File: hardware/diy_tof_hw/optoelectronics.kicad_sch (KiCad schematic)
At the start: 39 parts, among them IC21 74LVC1G08QW5-7, IC22 LMG1025QDEETQ1, SW2 SW_Nidec_CAS-120A1, U2 OPA858xDSG, U3 TLV3501AIDBV

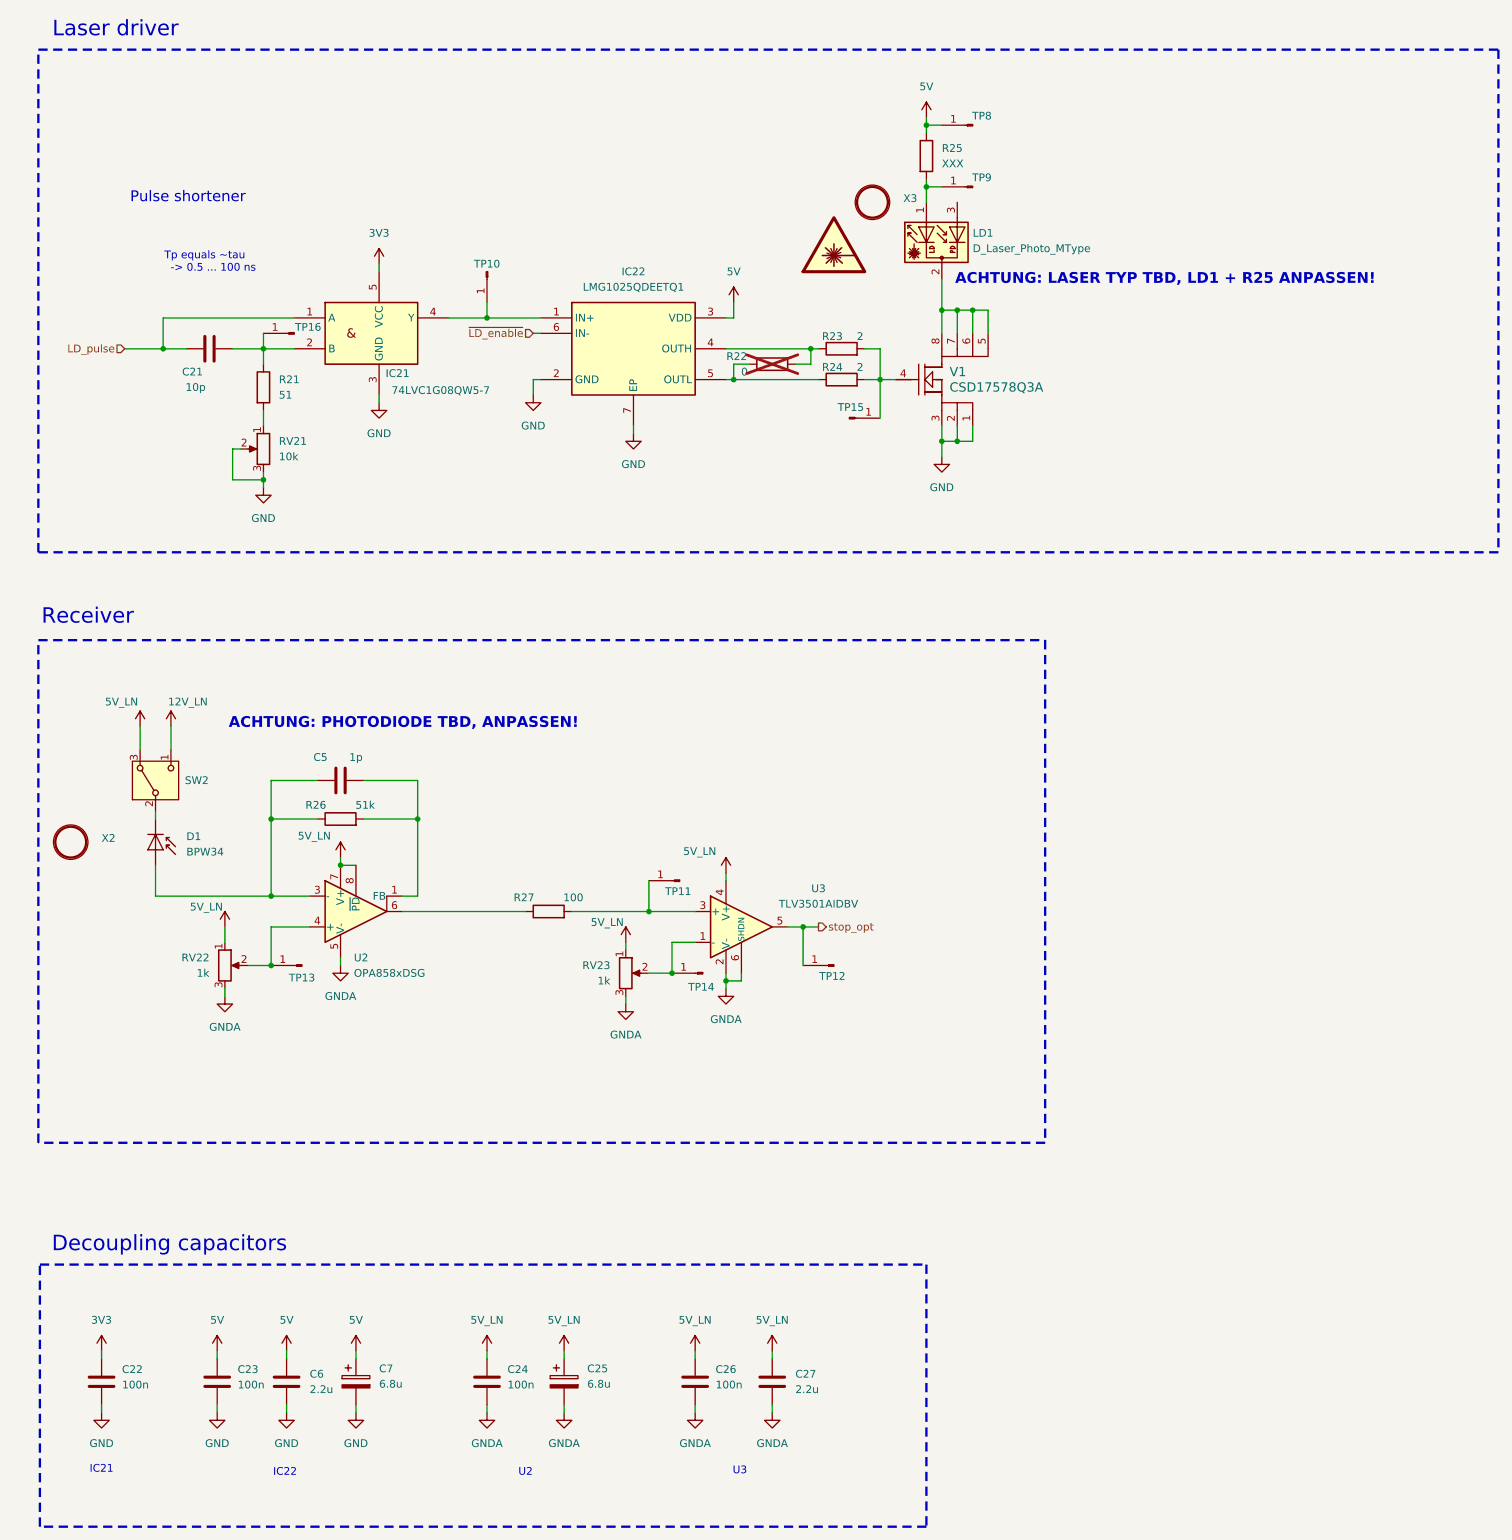
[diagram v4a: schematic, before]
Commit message: [hardware] added VCSEL, photodiode and some pcb graphics to the project
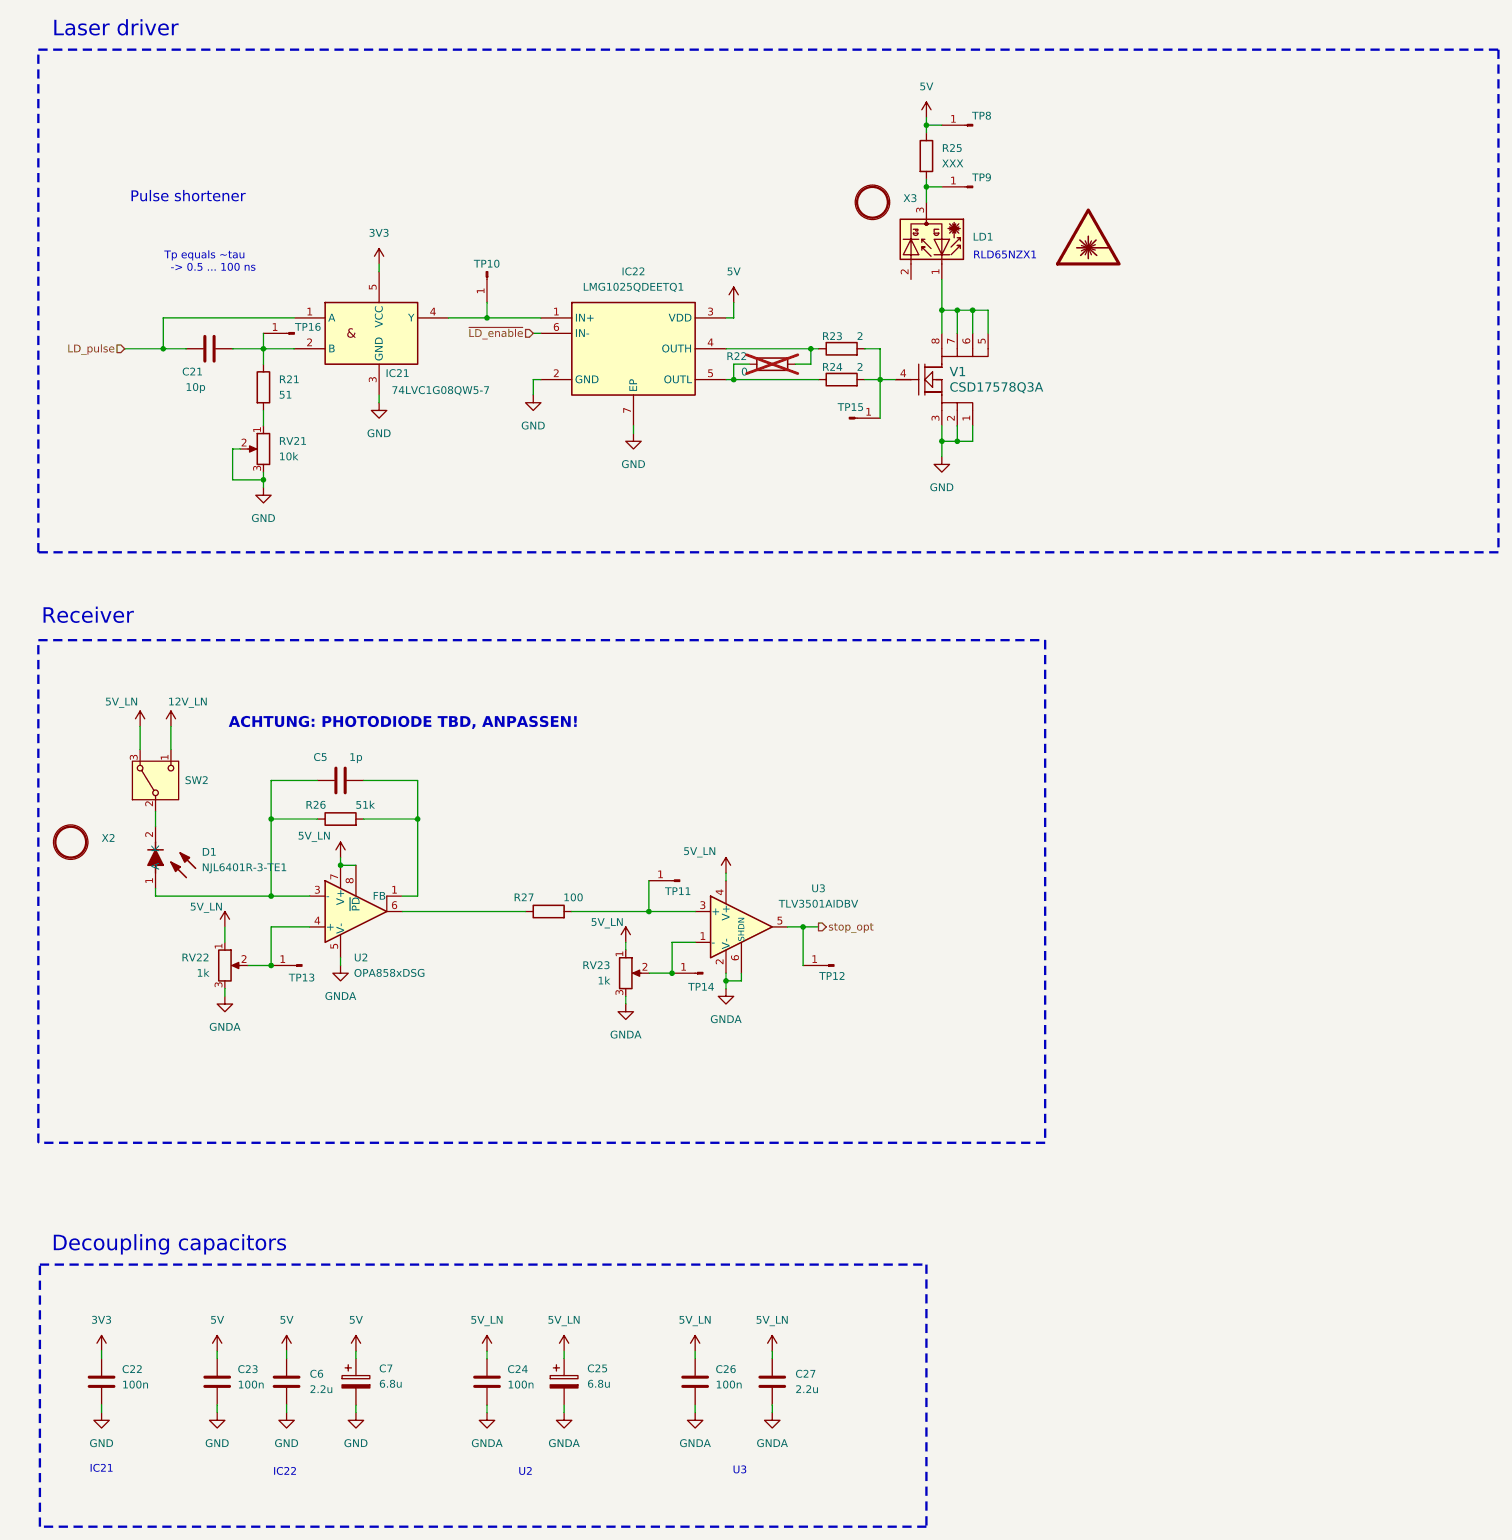
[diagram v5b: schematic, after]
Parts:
- removed D1: BPW34, OptoDevice:Osram_DIL2_4.3x4.65mm_P5.08mm, symbol Sensor_Optical:BPW34
- removed LD1: D_Laser_Photo_MType, OptoDevice:LaserDiode_TO5-D9-3, symbol Device:D_Laser_Photo_MType
- added D1: NJL6401R-3-TE1, NJL6401R3TE1, symbol NJL6401R-3-TE1:NJL6401R-3-TE1
- added LD1: ~, RLD65NZX1-00A:RLD85PZJ400A, symbol RLD65NZX1-00A:RLD65NZX1
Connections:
- net at C5.1, R26.1, U2.3 (-): now also D1.1 (A)
- net at SW2.2 (B): now also D1.2 (K)
- net at R25.2, TP9.1 (Pin_1): now also LD1.3
- net at V1.5, V1.6, V1.7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: now also LD1.1
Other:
- note added: "RLD65NZX1"
- note removed: "ACHTUNG: LASER TYP TBD, LD1 + R25 ANPASSEN!"
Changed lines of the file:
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@@
 	(wire
 		(pts
-			(xy 66.04 144.78) (xy 66.04 146.05)
+			(xy 66.04 144.78) (xy 66.04 147.32)
 		)
 		(stroke
@@
 	(wire
 		(pts
-			(xy 66.04 153.67) (xy 66.04 158.75)
-		)
-		(stroke
-			(width 0)
-			(type default)
-		)
-	)
-	(wire
-		(pts
 			(xy 173.99 68.58) (xy 175.26 68.58)
 		)
@@
 	(wire
 		(pts
+			(xy 66.04 157.48) (xy 66.04 158.75)
+		)
+		(stroke
+			(width 0)
+			(type default)
+		)
+	)
+	(wire
+		(pts
 			(xy 198.12 83.82) (xy 195.58 83.82)
 		)
@@
 		)
 	)
-	(text "ACHTUNG: LASER TYP TBD, LD1 + R25 ANPASSEN!"
-		(exclude_from_sim no)
-		(at 232.41 57.15 0)
-		(effects
-			(font
-				(size 1.778 1.778)
-				(thickness 0.3556)
-				(bold yes)
-				(color 255 36 34 1)
-			)
-		)
-	)
 	(text "U2"
 		(exclude_from_sim no)
@@
 		)
 	)
+	(text "RLD65NZX1"
+		(exclude_from_sim no)
+		(at 205.994 53.34 0)
+		(effects
+			(font
+				(size 1.27 1.27)
+			)
+		)
+	)
 	(text "IC22"
 		(exclude_from_sim no)
@@
 	)
 	(symbol
+		(lib_id "RLD65NZX1-00A:RLD65NZX1")
+		(at 193.04 50.8 270)
+		(unit 1)
+		(exclude_from_sim no)
+		(in_bom yes)
+		(on_board yes)
+		(dnp no)
+		(fields_autoplaced yes)
+		(property "Reference" "LD1"
+			(at 200.66 50.1649 90)
+			(effects
+				(font
+					(size 1.27 1.27)
+				)
+				(justify left)
+			)
+		)
+		(property "Value" "~"
+			(at 200.66 52.07 90)
+			(effects
+				(font
+					(size 1.27 1.27)
+				)
+				(justify left)
+			)
+		)
+		(property "Footprint" "RLD65NZX1-00A:RLD85PZJ400A"
+			(at 193.04 50.8 0)
+			(effects
+				(font
+					(size 1.27 1.27)
+				)
+				(hide yes)
+			)
+		)
+		(property "Datasheet" ""
+			(at 193.04 50.8 0)
+			(effects
+				(font
+					(size 1.27 1.27)
+				)
+				(hide yes)
+			)
+		)
+		(property "Description" ""
+			(at 193.04 50.8 0)
+			(effects
+				(font
+					(size 1.27 1.27)
+				)
+				(hide yes)
+			)
+		)
+		(pin "1"
+		)
+		(pin "2"
+		)
+		(pin "3"
+		)
+		(instances
+			(project ""
+				(path "/0f7bf370-0a80-4101-a61d-d850fd66ab1d/1536e9f2-3315-42ae-af66-5ae730c43aea"
+					(reference "LD1")
+					(unit 1)
+				)
+			)
+		)
+	)
+	(symbol
 		(lib_id "Device:C")
 		(at 154.94 238.76 0)
@@
 	)
 	(symbol
-		(lib_id "Sensor_Optical:BPW34")
-		(at 66.04 151.13 270)
-		(unit 1)
-		(exclude_from_sim no)
-		(in_bom yes)
-		(on_board yes)
-		(dnp no)
-		(fields_autoplaced yes)
-		(property "Reference" "D1"
-			(at 71.12 148.9328 90)
-			(effects
-				(font
-					(size 1.27 1.27)
-				)
-				(justify left)
-			)
-		)
-		(property "Value" "BPW34"
-			(at 71.12 151.4728 90)
-			(effects
-				(font
-					(size 1.27 1.27)
-				)
-				(justify left)
-			)
-		)
-		(property "Footprint" "OptoDevice:Osram_DIL2_4.3x4.65mm_P5.08mm"
-			(at 70.485 151.13 0)
-			(effects
-				(font
-					(size 1.27 1.27)
-				)
-				(hide yes)
-			)
-		)
-		(property "Datasheet" "http://www.vishay.com/docs/81521/bpw34.pdf"
-			(at 66.04 149.86 0)
-			(effects
-				(font
-					(size 1.27 1.27)
-				)
-				(hide yes)
-			)
-		)
-		(property "Description" "Silicon PIN Photodiode"
-			(at 66.04 151.13 0)
-			(effects
-				(font
-					(size 1.27 1.27)
-				)
-				(hide yes)
-			)
-		)
-		(pin "1"
-		)
-		(pin "2"
-		)
-		(instances
-			(project "diy_tof_hw"
-				(path "/0f7bf370-0a80-4101-a61d-d850fd66ab1d/1536e9f2-3315-42ae-af66-5ae730c43aea"
-					(reference "D1")
-					(unit 1)
-				)
-			)
-		)
-	)
-	(symbol
 		(lib_id "Connector:Conn_01x01_Pin")
 		(at 120.65 55.88 270)
@@
 	)
 	(symbol
-		(lib_id "Device:D_Laser_Photo_MType")
-		(at 195.58 52.07 90)
-		(unit 1)
-		(exclude_from_sim no)
-		(in_bom yes)
-		(on_board yes)
-		(dnp no)
-		(property "Reference" "LD1"
-			(at 200.66 49.5299 90)
-			(effects
-				(font
-					(size 1.27 1.27)
-				)
-				(justify right)
-			)
-		)
-		(property "Value" "D_Laser_Photo_MType"
-			(at 200.66 52.0699 90)
-			(effects
-				(font
-					(size 1.27 1.27)
-				)
-				(justify right)
-			)
-		)
-		(property "Footprint" "OptoDevice:LaserDiode_TO5-D9-3"
-			(at 193.675 51.054 0)
-			(effects
-				(font
-					(size 1.27 1.27)
-				)
-				(hide yes)
-			)
-		)
-		(property "Datasheet" "http://www.egismos.disonhu.com/laser/diode-package.htm"
-			(at 198.12 49.784 0)
-			(effects
-				(font
-					(size 1.27 1.27)
-				)
-				(hide yes)
-			)
-		)
-		(property "Description" "Laser diode with photodiode, common cathode on pin 2"
-			(at 195.58 52.07 0)
-			(effects
-				(font
-					(size 1.27 1.27)
-				)
-				(hide yes)
-			)
-		)
-		(pin "1"
-		)
-		(pin "2"
-		)
-		(pin "3"
-		)
-		(instances
-			(project ""
-				(path "/0f7bf370-0a80-4101-a61d-d850fd66ab1d/1536e9f2-3315-42ae-af66-5ae730c43aea"
-					(reference "LD1")
-					(unit 1)
-				)
-			)
-		)
-	)
-	(symbol
 		(lib_id "power:GNDA")
 		(at 167.64 243.84 0)
@@
 	)
 	(symbol
+		(lib_id "NJL6401R-3-TE1:NJL6401R-3-TE1")
+		(at 66.04 157.48 180)
+		(unit 1)
+		(exclude_from_sim no)
+		(in_bom yes)
+		(on_board yes)
+		(dnp no)
+		(fields_autoplaced yes)
+		(property "Reference" "D1"
+			(at 73.66 151.5109 0)
+			(effects
+				(font
+					(size 1.27 1.27)
+				)
+				(justify right)
+			)
+		)
+		(property "Value" "NJL6401R-3-TE1"
+			(at 73.66 154.0509 0)
+			(effects
+				(font
+					(size 1.27 1.27)
+				)
+				(justify right)
+			)
+		)
+		(property "Footprint" "NJL6401R3TE1"
+			(at 62.738 51.13 0)
+			(effects
+				(font
+					(size 1.27 1.27)
+				)
+				(justify left top)
+				(hide yes)
+			)
+		)
+		(property "Datasheet" "https://componentsearchengine.com/Datasheets/1/NJL6401R-3-TE1.pdf"
+			(at 62.738 -48.87 0)
+			(effects
+				(font
+					(size 1.27 1.27)
+				)
+				(justify left top)
+				(hide yes)
+			)
+		)
+		(property "Description" "Photodiode 800nm 2ns 2-SMD, No Lead"
+			(at 66.04 157.48 0)
+			(effects
+				(font
+					(size 1.27 1.27)
+				)
+				(hide yes)
+			)
+		)
+		(property "Height" "0.95"
+			(at 62.738 -248.87 0)
+			(effects
+				(font
+					(size 1.27 1.27)
+				)
+				(justify left top)
+				(hide yes)
+			)
+		)
+		(property "Mouser Part Number" "513-NJL6401R-3-TE1"
+			(at 62.738 -348.87 0)
+			(effects
+				(font
+					(size 1.27 1.27)
+				)
+				(justify left top)
+				(hide yes)
+			)
+		)
+		(property "Mouser Price/Stock" "https://www.mouser.com/Search/Refine.aspx?Keyword=513-NJL6401R-3-TE1"
+			(at 62.738 -448.87 0)
+			(effects
+				(font
+					(size 1.27 1.27)
+				)
+				(justify left top)
+				(hide yes)
+			)
+		)
+		(property "Manufacturer_Name" "New Japan Radio"
+			(at 62.738 -548.87 0)
+			(effects
+				(font
+					(size 1.27 1.27)
+				)
+				(justify left top)
+				(hide yes)
+			)
+		)
+		(property "Manufacturer_Part_Number" "NJL6401R-3-TE1"
+			(at 62.738 -648.87 0)
+			(effects
+				(font
+					(size 1.27 1.27)
+				)
+				(justify left top)
+				(hide yes)
+			)
+		)
+		(pin "2"
+		)
+		(pin "1"
+		)
+		(instances
+			(project ""
+				(path "/0f7bf370-0a80-4101-a61d-d850fd66ab1d/1536e9f2-3315-42ae-af66-5ae730c43aea"
+					(reference "D1")
+					(unit 1)
+				)
+			)
+		)
+	)
+	(symbol
 		(lib_id "User_Library:Qioptiq_Mount")
 		(at 52.07 149.86 0)
@@
 	(symbol
 		(lib_id "Graphic:SYM_LASER_Large")
-		(at 177.8 50.8 0)
+		(at 219.71 49.53 0)
 		(unit 1)
 		(exclude_from_sim yes)
@@
 		(fields_autoplaced yes)
 		(property "Reference" "#SYM2"
-			(at 177.8 45.72 0)
+			(at 219.71 44.45 0)
 			(effects
 				(font
@@
 		)
 		(property "Value" "SYM_LASER_Large"
-			(at 177.8 57.531 0)
+			(at 219.71 56.261 0)
 			(effects
 				(font
@@
 		)
 		(property "Footprint" ""
-			(at 177.546 55.245 0)
+			(at 219.456 53.975 0)
 			(effects
 				(font
@@
 		)
 		(property "Datasheet" "~"
-			(at 178.562 55.88 0)
+			(at 220.472 54.61 0)
 			(effects
 				(font
@@
 		)
 		(property "Description" "Laser radiation warning symbol, large"
-			(at 177.8 50.8 0)
+			(at 219.71 49.53 0)
 			(effects
 				(font
